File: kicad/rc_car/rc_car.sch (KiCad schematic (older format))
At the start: 30 parts

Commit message: [kicad] schematic and layout done
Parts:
- removed C?: 10u, symbol Device:CP1
- removed C?: 100n, symbol Device:C
- removed J?: Screw_Terminal_01x02, symbol Connector:Screw_Terminal_01x02
- added C8: 100n, Capacitor_SMD:C_0805_2012Metric, symbol Device:C
- added unit 5 of U1
- C1, C4: renamed from C?; footprint (none) -> Capacitor_THT:CP_Radial_D6.3mm_P2.50mm
- C2, C3, C5: renamed from C?; footprint (none) -> Capacitor_SMD:C_0805_2012Metric
- D1, D2: renamed from D?; footprint (none) -> LED_THT:LED_D3.0mm
- J1: renamed from J?; footprint (none) -> Connector_PinHeader_2.54mm:PinHeader_2x20_P2.54mm_Vertical
- J3: renamed from J?; footprint (none) -> Connector_Wire:SolderWirePad_1x02_P5.08mm_Drill1.5mm
- J4, J5, J6: renamed from J?; footprint (none) -> Connector_PinHeader_2.54mm:PinHeader_1x03_P2.54mm_Horizontal
- J7, J8: renamed from J?; footprint (none) -> Connector_PinHeader_2.54mm:PinHeader_1x04_P2.54mm_Vertical
- JP1: renamed from JP?; footprint (none) -> Connector_PinHeader_2.54mm:PinHeader_1x02_P2.54mm_Vertical
- R1, R2, R3, R4, R5, R6, R7, R8: renamed from R?; footprint (none) -> Resistor_SMD:R_0805_2012Metric
- SW1: renamed from SW?; footprint (none) -> Button_Switch_THT:SW_PUSH_6mm; symbol Switch:SW_Push_Dual -> Switch:SW_Push
- gave numbers to parts that had none: 3
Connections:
- net !reset: now also A1.28 (~RESET); no longer A1.3 (~RESET)
- net +3V3: now also J1.1 (3V3)
- net GND: now also J1.14 (GND), J1.20 (GND), J1.25 (GND), J1.30 (GND), J1.34 (GND), J1.39 (GND), J1.9 (GND), SW1.2, C8.2, U1.7 (VSS); no longer SW1.4
- net VCC: now also J1.4 (5V), C8.1, U1.14 (VDD)
- net button: now also SW1.1; no longer SW1.3
- net rxd: now also J7.3 (Pin_3); no longer J7.2 (Pin_2)
- net txd: now also J7.2 (Pin_2); no longer J7.3 (Pin_3)
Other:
- moved on the sheet: A1, C3, C4, C5, J4, J5, J6

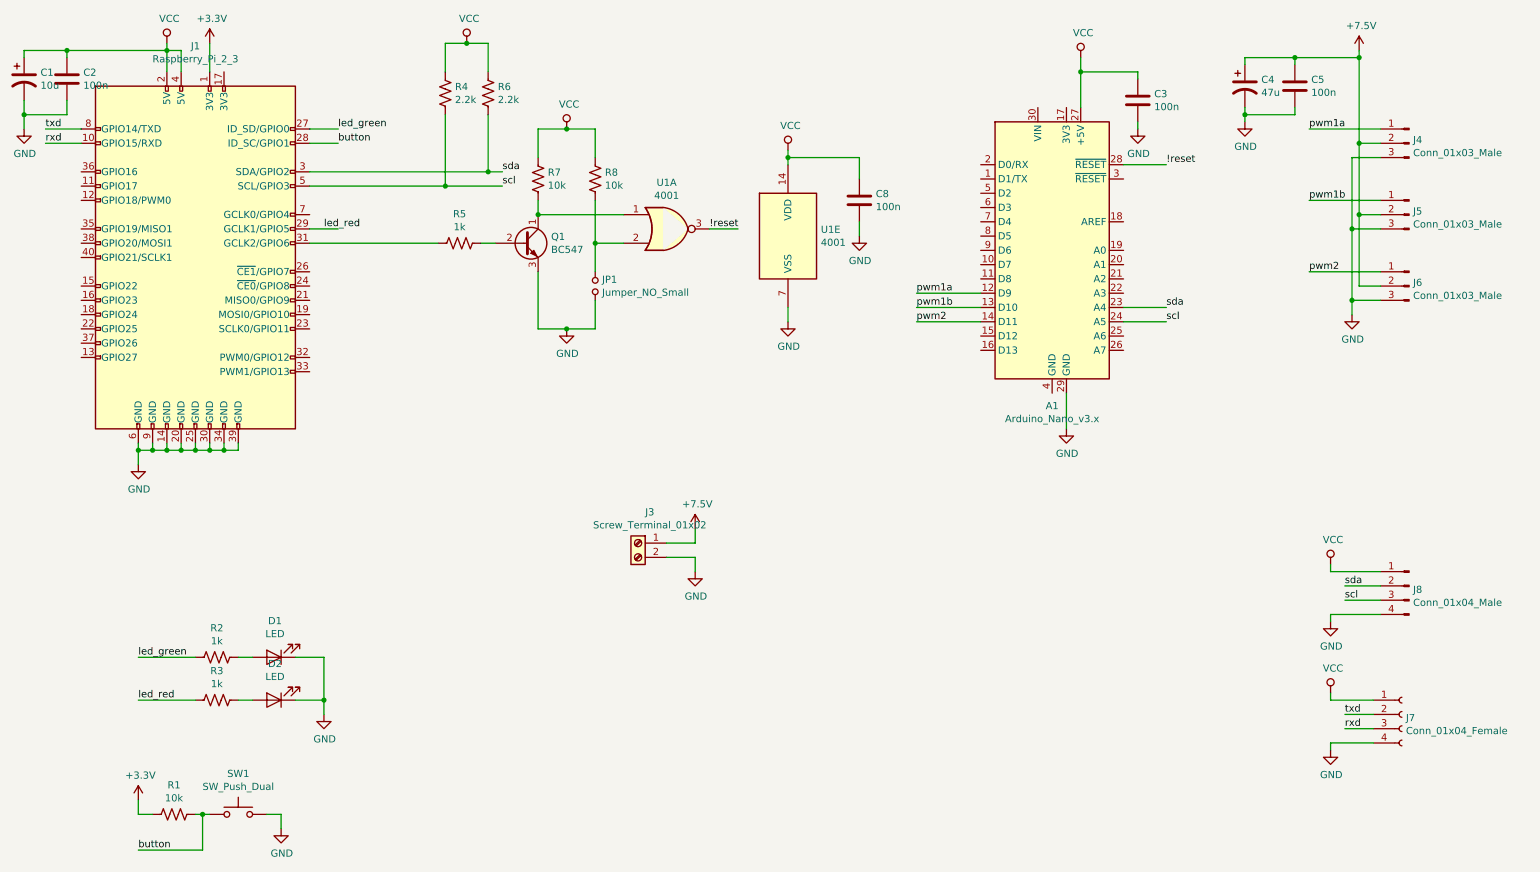
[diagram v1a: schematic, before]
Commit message: [kicad/rc_car] wired pins of the atmega to some connectors
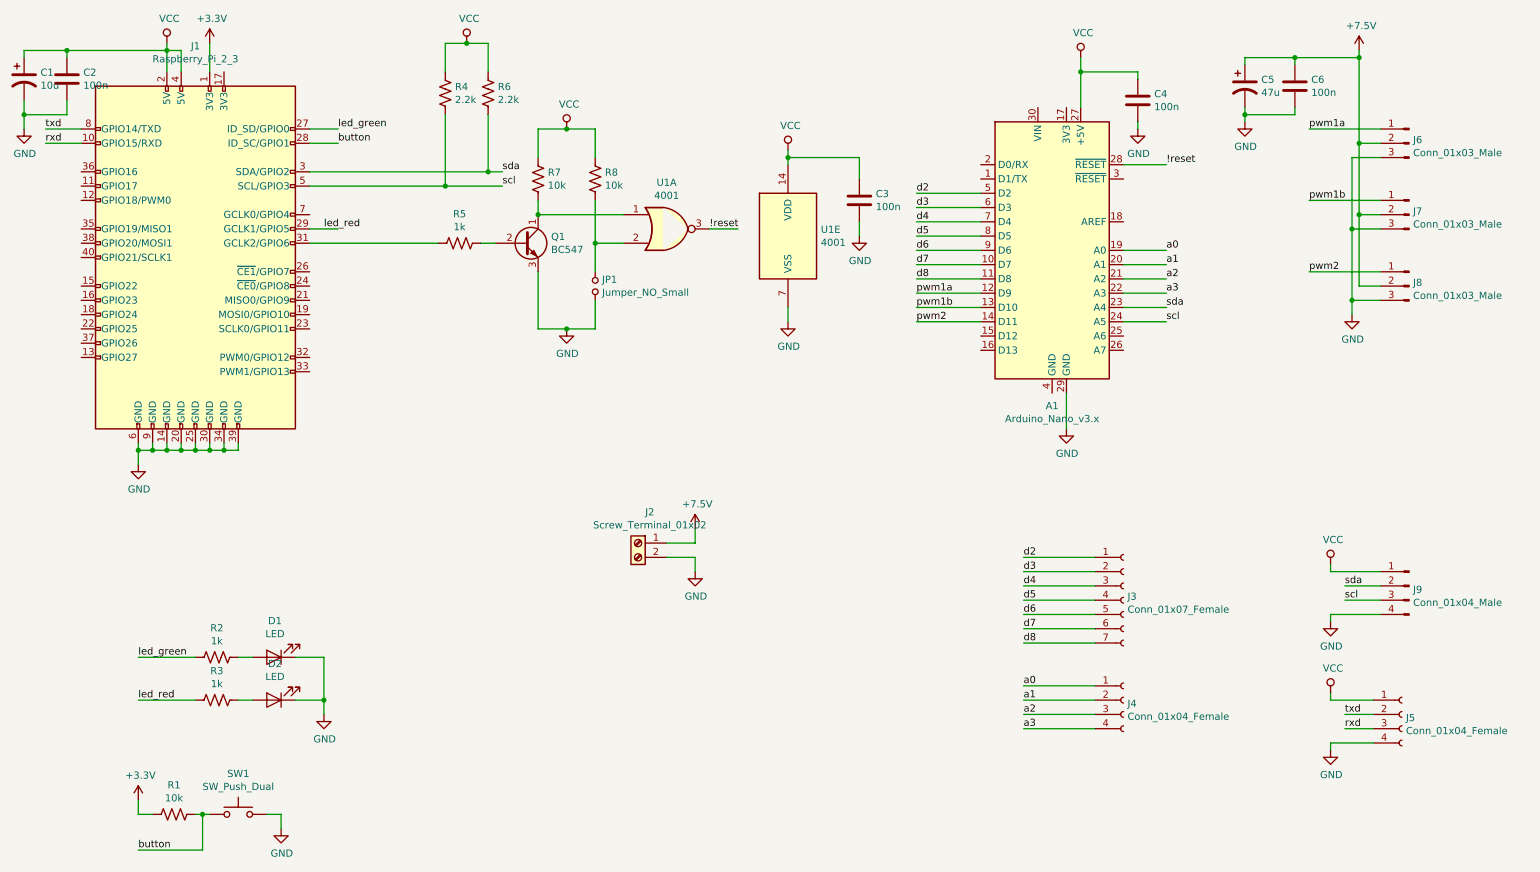
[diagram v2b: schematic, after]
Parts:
- added J3: Conn_01x07_Female, Connector_PinHeader_2.54mm:PinHeader_1x07_P2.54mm_Vertical, symbol Connector:Conn_01x07_Female
- added J4: Conn_01x04_Female, Connector_PinHeader_2.54mm:PinHeader_1x04_P2.54mm_Vertical, symbol Connector:Conn_01x04_Female
- U1: footprint (none) -> Package_DIP:DIP-14_W7.62mm_Socket_LongPads
- renumbered C8 to C3, C3 to C4, C4 to C5, C5 to C6, J3 to J2, J7 to J5, J4 to J6, J5 to J7, J6 to J8, J8 to J9
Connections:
- net d7: now reaches A1.10 (D7)
- net d7: now also J3.6 (Pin_6)
- net d8: now reaches A1.11 (D8)
- net d8: now also J3.7 (Pin_7)
- net a0: now reaches A1.19 (A0)
- net a0: now also J4.1 (Pin_1)
- net a1: now reaches A1.20 (A1)
- net a1: now also J4.2 (Pin_2)
- net a2: now reaches A1.21 (A2)
- net a2: now also J4.3 (Pin_3)
- net a3: now reaches A1.22 (A3)
- net a3: now also J4.4 (Pin_4)
- net d2: now reaches A1.5 (D2)
- net d2: now also J3.1 (Pin_1)
- net d3: now reaches A1.6 (D3)
- net d3: now also J3.2 (Pin_2)
- net d4: now reaches A1.7 (D4)
- net d4: now also J3.3 (Pin_3)
- net d5: now reaches A1.8 (D5)
- net d5: now also J3.4 (Pin_4)
- net d6: now reaches A1.9 (D6)
- net d6: now also J3.5 (Pin_5)
